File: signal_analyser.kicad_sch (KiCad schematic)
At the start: 0 parts

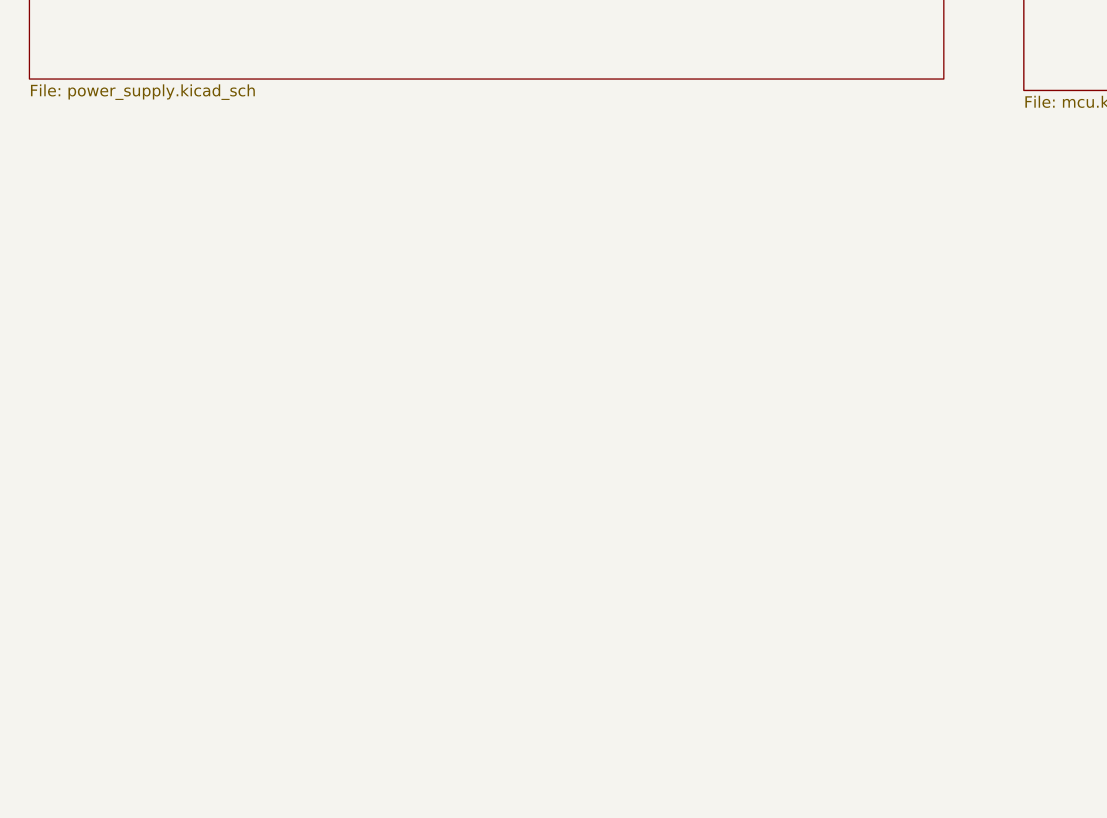
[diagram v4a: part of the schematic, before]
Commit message: Added 14-bit s/h ADC
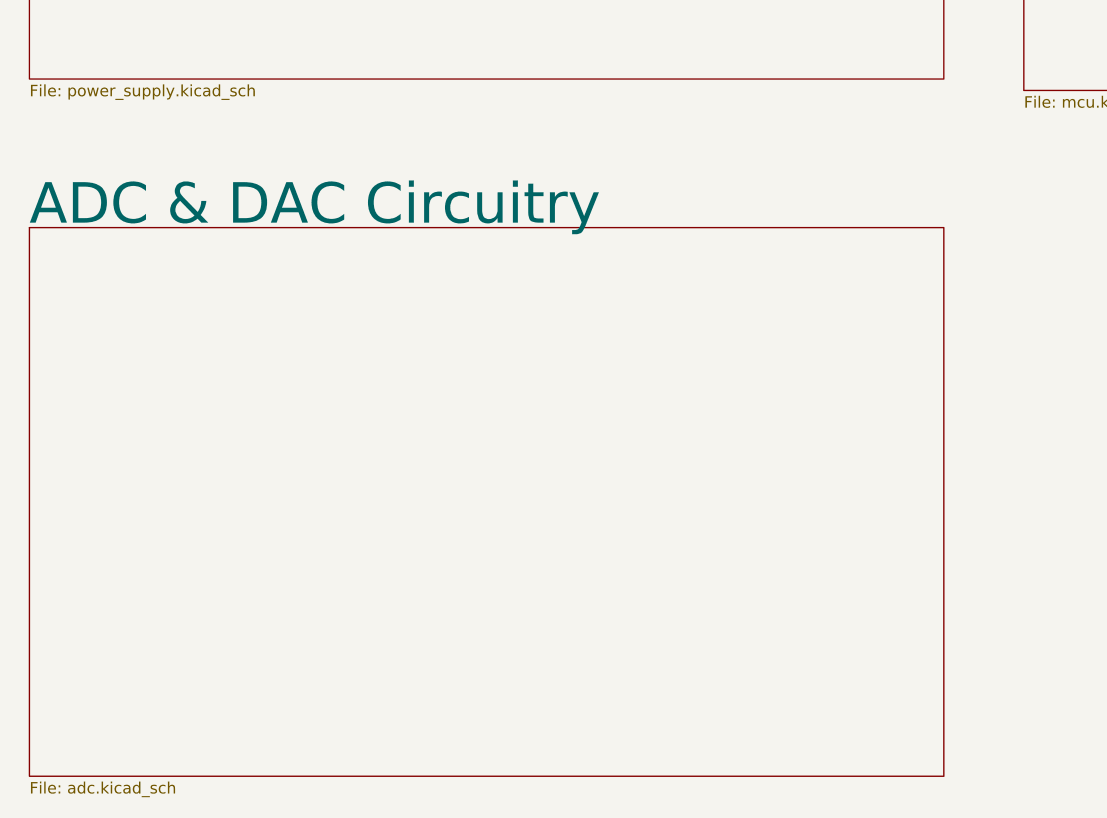
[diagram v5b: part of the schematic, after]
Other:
- added sheet ADC & DAC Circuitry (adc.kicad_sch)
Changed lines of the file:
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@@
+    )
+  )
+  (sheet (at 38.1 118.11) (size 101.6 60.96)
+    (stroke (width 0.1524) (type solid) (color 0 0 0 0))
+    (fill (color 0 0 0 0.0000))
+    (property "Sheet name" "ADC & DAC Circuitry" (id 0) (at 38.1 118.11 0)
+      (effects (font (size 4.5 4.5)) (justify left bottom))
+    )
+    (property "Sheet file" "adc.kicad_sch" (id 1) (at 38.1 179.6546 0)
+      (effects (font (size 1.27 1.27)) (justify left top))
     )
   )
@@
     (path "/00000000-0000-0000-0000-000061f3b48b" (page "2"))
     (path "/eccad5a0-ddbd-4a3e-af28-d21812660dc8" (page "3"))
+    (path "/a826d4f1-aa41-4d34-8070-125b5f8ee214" (page "4"))
   )
   (symbol_instances
@@
       (reference "#PWR?") (unit 1) (value "+3.3VA") (footprint "")
     )
+    (path "/a826d4f1-aa41-4d34-8070-125b5f8ee214/0a0fb63b-fe02-4679-b8d3-7d9410a5912d"
+      (reference "#PWR?") (unit 1) (value "GND") (footprint "")
+    )
+    (path "/a826d4f1-aa41-4d34-8070-125b5f8ee214/0df58b8d-6cc2-44ab-91ac-38a4b262177b"
+      (reference "#PWR?") (unit 1) (value "+3.3VA") (footprint "")
+    )
     (path "/eccad5a0-ddbd-4a3e-af28-d21812660dc8/13b3a07b-b545-442a-bd9d-8407b02a0fa1"
       (reference "#PWR?") (unit 1) (value "GND") (footprint "")
@@
       (reference "#PWR?") (unit 1) (value "VCOM") (footprint "")
     )
+    (path "/a826d4f1-aa41-4d34-8070-125b5f8ee214/2c0b223e-26db-4789-986d-2fc3cbd1a6ea"
+      (reference "#PWR?") (unit 1) (value "GND") (footprint "")
+    )
     (path "/eccad5a0-ddbd-4a3e-af28-d21812660dc8/3a73d96a-6eec-4460-81e8-ea81dead193a"
       (reference "#PWR?") (unit 1) (value "GND") (footprint "")
@@
       (reference "#PWR?") (unit 1) (value "+3.3VA") (footprint "")
     )
+    (path "/a826d4f1-aa41-4d34-8070-125b5f8ee214/44497b76-cfe7-4c21-a33b-c1b3dc63ff6d"
+      (reference "#PWR?") (unit 1) (value "+3V3") (footprint "")
+    )
+    (path "/a826d4f1-aa41-4d34-8070-125b5f8ee214/483316c9-cf0a-4b38-93d3-819516b8b654"
+      (reference "#PWR?") (unit 1) (value "GND") (footprint "")
+    )
     (path "/eccad5a0-ddbd-4a3e-af28-d21812660dc8/49ace869-9b77-46c3-93e0-d59f5f95d777"
       (reference "#PWR?") (unit 1) (value "GND") (footprint "")
+    )
+    (path "/a826d4f1-aa41-4d34-8070-125b5f8ee214/56d106cf-55de-4151-8d92-a03bffa1cddf"
+      (reference "#PWR?") (unit 1) (value "+5V") (footprint "")
     )
     (path "/00000000-0000-0000-0000-000061f3b48b/620d5fb2-47c5-4a7a-872e-e9f873c5a897"
       (reference "#PWR?") (unit 1) (value "+5V") (footprint "")
     )
+    (path "/a826d4f1-aa41-4d34-8070-125b5f8ee214/63633205-6bdd-4747-81c5-d10942a82e10"
+      (reference "#PWR?") (unit 1) (value "GND") (footprint "")
+    )
     (path "/eccad5a0-ddbd-4a3e-af28-d21812660dc8/6711a80d-d88b-4950-ae79-c51aa5a13b51"
       (reference "#PWR?") (unit 1) (value "VBUS") (footprint "")
@@
       (reference "#PWR?") (unit 1) (value "GND") (footprint "")
     )
+    (path "/a826d4f1-aa41-4d34-8070-125b5f8ee214/758c4631-a73d-46a9-a404-1980bcba4656"
+      (reference "#PWR?") (unit 1) (value "GND") (footprint "")
+    )
     (path "/eccad5a0-ddbd-4a3e-af28-d21812660dc8/77295f54-9876-4121-b1d4-6b961536abe9"
       (reference "#PWR?") (unit 1) (value "+3V3") (footprint "")
@@
       (reference "C?") (unit 1) (value "22u") (footprint "")
     )
+    (path "/a826d4f1-aa41-4d34-8070-125b5f8ee214/0d41fe7f-f192-4084-8462-0c98edfb0a88"
+      (reference "C?") (unit 1) (value "0.1u") (footprint "")
+    )
     (path "/eccad5a0-ddbd-4a3e-af28-d21812660dc8/0f147e98-234c-4dfd-8a4e-b4693160b73d"
       (reference "C?") (unit 1) (value "100n") (footprint "")
@@
       (reference "C?") (unit 1) (value "100n") (footprint "")
     )
+    (path "/a826d4f1-aa41-4d34-8070-125b5f8ee214/49ab8af4-7d65-404d-a549-639845d6c835"
+      (reference "C?") (unit 1) (value "0.1u") (footprint "")
+    )
     (path "/eccad5a0-ddbd-4a3e-af28-d21812660dc8/57137efd-14f1-4e31-9fb4-6ba23f92039a"
       (reference "C?") (unit 1) (value "100n") (footprint "")
+    )
+    (path "/a826d4f1-aa41-4d34-8070-125b5f8ee214/57849295-d364-4182-b693-103642d2aae6"
+      (reference "C?") (unit 1) (value "10u") (footprint "")
     )
     (path "/eccad5a0-ddbd-4a3e-af28-d21812660dc8/61314be0-63e8-42fd-89f0-fa9d6d3c5636"
@@
       (reference "C?") (unit 1) (value "10p") (footprint "")
     )
+    (path "/a826d4f1-aa41-4d34-8070-125b5f8ee214/838e52c2-25b4-4983-87dd-a77d47551f01"
+      (reference "C?") (unit 1) (value "10u") (footprint "")
+    )
     (path "/eccad5a0-ddbd-4a3e-af28-d21812660dc8/8969c368-9450-49fd-9efc-0e8562dc0033"
       (reference "C?") (unit 1) (value "1u") (footprint "")
@@
       (reference "C?") (unit 1) (value "10p") (footprint "")
     )
+    (path "/a826d4f1-aa41-4d34-8070-125b5f8ee214/9e994efc-68a3-4464-985b-11603562e64b"
+      (reference "C?") (unit 1) (value "10u") (footprint "")
+    )
+    (path "/a826d4f1-aa41-4d34-8070-125b5f8ee214/b22b8c9e-dd4f-4431-92de-c8167af15ac6"
+      (reference "C?") (unit 1) (value "0.1u") (footprint "")
+    )
     (path "/eccad5a0-ddbd-4a3e-af28-d21812660dc8/b469e189-be9e-4478-ab0a-62b1edcf3e48"
       (reference "C?") (unit 1) (value "100n") (footprint "")
@@
     (path "/eccad5a0-ddbd-4a3e-af28-d21812660dc8/b5a3aabe-c57d-4f24-b844-400086efa7a3"
       (reference "C?") (unit 1) (value "100n") (footprint "")
+    )
+    (path "/a826d4f1-aa41-4d34-8070-125b5f8ee214/ce31ed08-2d9f-4873-8660-3e7ab7214fb1"
+      (reference "C?") (unit 1) (value "10u") (footprint "")
+    )
+    (path "/a826d4f1-aa41-4d34-8070-125b5f8ee214/dc9eb6fc-4822-42e6-a7e2-e8d278443d60"
+      (reference "C?") (unit 1) (value "10u") (footprint "")
     )
     (path "/eccad5a0-ddbd-4a3e-af28-d21812660dc8/f2632247-31a5-4afb-a76b-8ec7549dc9ef"
@@
       (reference "R?") (unit 1) (value "49R9") (footprint "")
     )
+    (path "/a826d4f1-aa41-4d34-8070-125b5f8ee214/0ecef775-00d7-45a6-8f62-83e8dfb28e36"
+      (reference "R?") (unit 1) (value "49R9") (footprint "")
+    )
     (path "/00000000-0000-0000-0000-000061f3b48b/1a0644fc-0f2d-4bfb-9b50-cfb250157a5e"
       (reference "R?") (unit 1) (value "1k") (footprint "")
+    )
+    (path "/a826d4f1-aa41-4d34-8070-125b5f8ee214/279e86f6-cbba-4b10-85b8-3fe9f875a9f1"
+      (reference "R?") (unit 1) (value "0") (footprint "")
     )
     (path "/eccad5a0-ddbd-4a3e-af28-d21812660dc8/4a9afb9d-248f-469c-b466-1f7da141cc1c"
@@
       (reference "U?") (unit 1) (value "STM32F103CBT6") (footprint "Package_QFP:LQFP-48_7x7mm_P0.5mm")
     )
+    (path "/a826d4f1-aa41-4d34-8070-125b5f8ee214/78e5508a-e5d9-4fa0-9f80-dc5b09689462"
+      (reference "U?") (unit 1) (value "ADC141S626") (footprint "")
+    )
+    (path "/a826d4f1-aa41-4d34-8070-125b5f8ee214/90628c49-7de1-4dd6-9f62-b3dd77a19e3f"
+      (reference "U?") (unit 1) (value "REF3033AIDBZT") (footprint "Package_TO_SOT_SMD:SOT-23")
+    )
     (path "/eccad5a0-ddbd-4a3e-af28-d21812660dc8/afc4f5d3-dc9b-4fd2-a95b-1f1b12d5dcab"

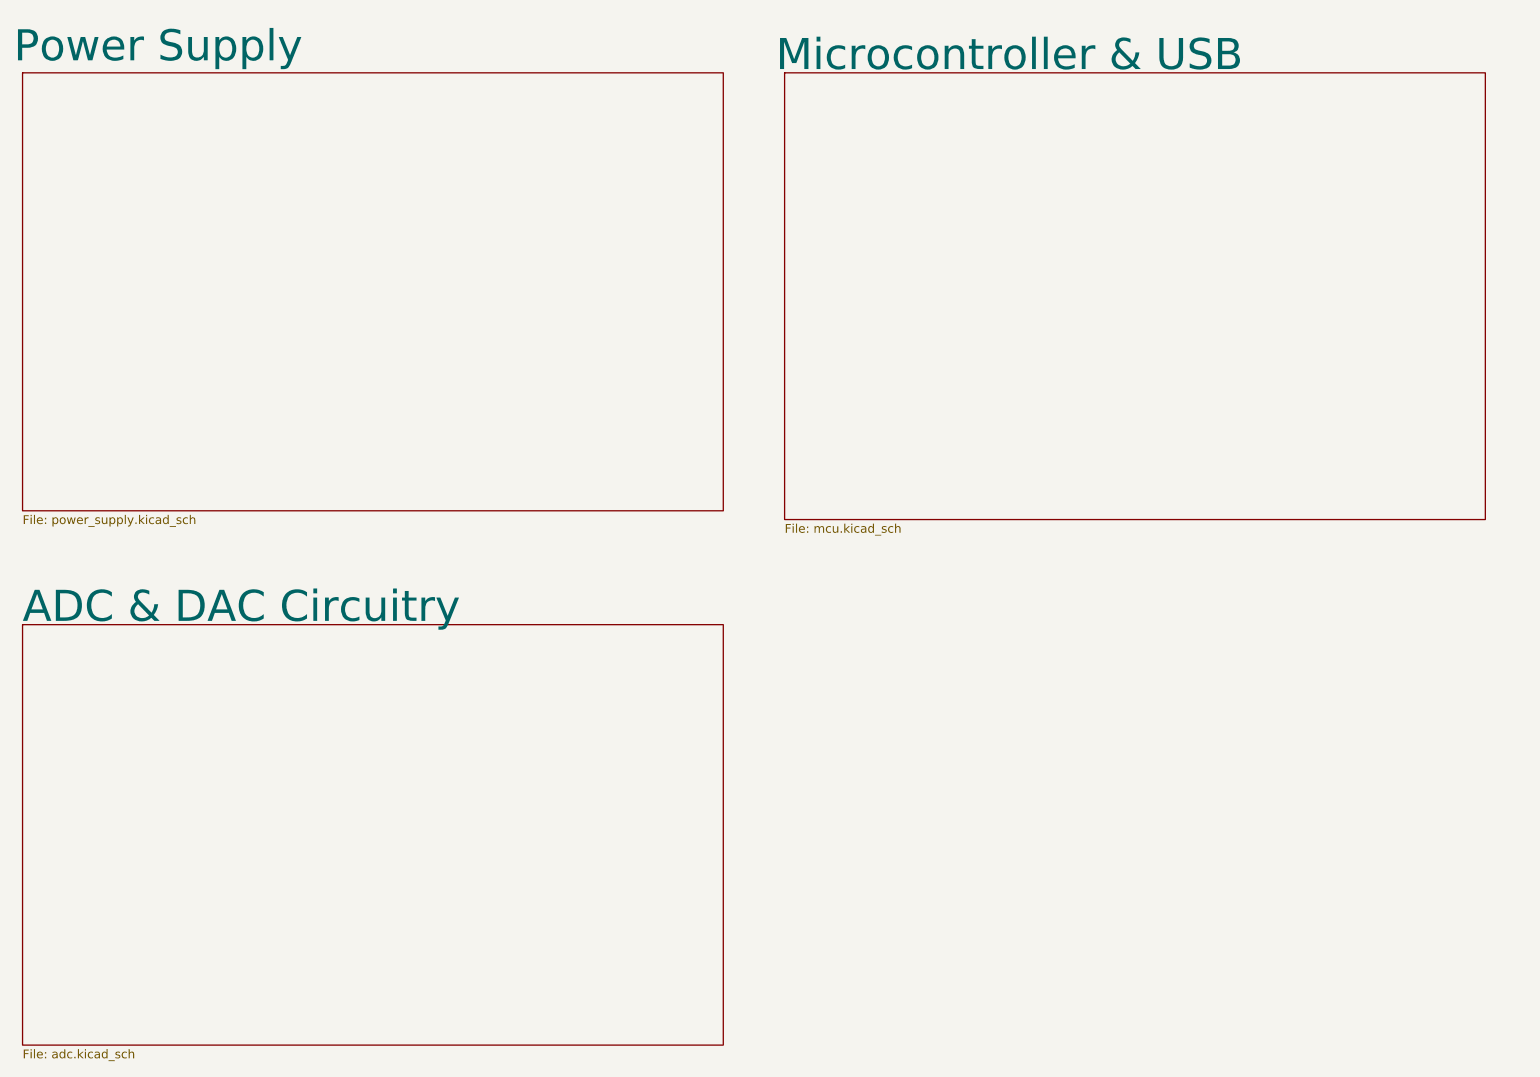
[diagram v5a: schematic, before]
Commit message: Completed ADC, DAC, Analogue In, and Analogue Out
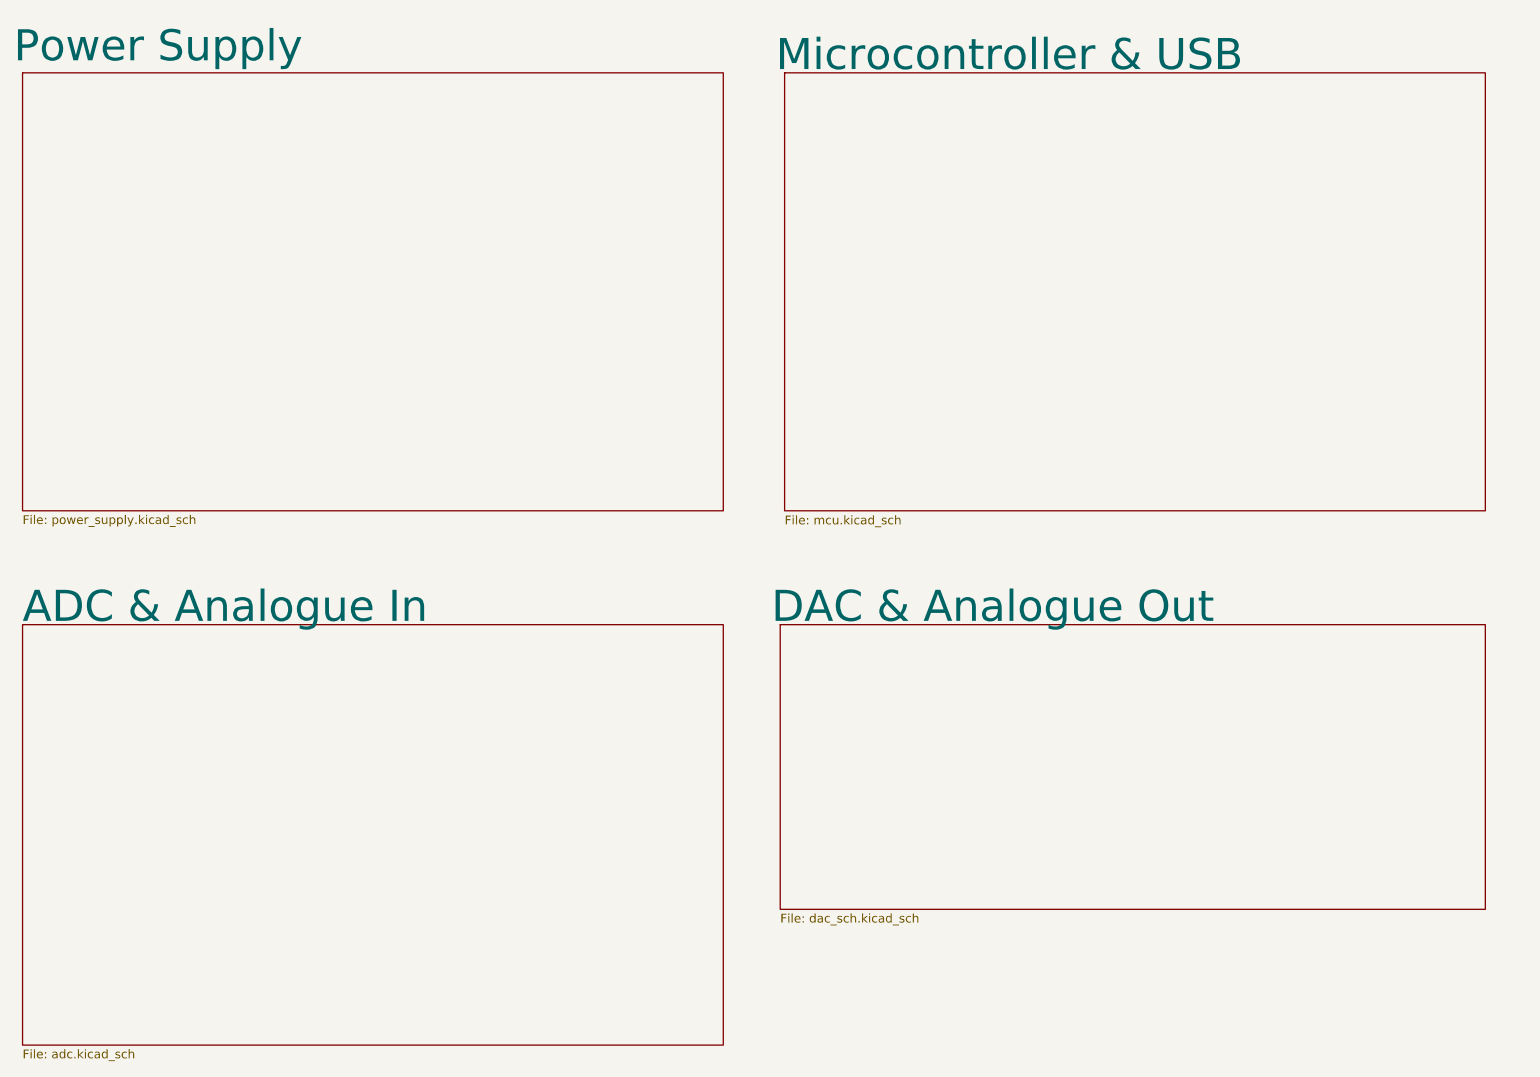
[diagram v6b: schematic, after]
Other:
- sheet ADC & DAC Circuitry renamed ADC & Analogue In
- added sheet DAC & Analogue Out (dac_sch.kicad_sch)

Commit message: ERC valid.
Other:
- sheet ADC & Analogue In renamed [3] ADC & Analogue In
- sheet DAC & Analogue Out renamed [4] DAC & Analogue Out
- sheet Microcontroller & USB renamed [2] Microcontroller & USB
- sheet Power Supply renamed [1] Power Supply
